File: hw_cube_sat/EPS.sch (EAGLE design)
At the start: 0 parts

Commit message: added sections for eps sch
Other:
- note added: "3V REFERENCE"
- note added: "3V3 REGULATOR"
- note added: "BATTERY + BATTERY CHARGER"
- note added: "HIGH-LEVEL ARCHITECTURE"
- note added: "POWER MANAGEMENT MICROCONTROLLER"
- note added: "SOLAR ARRAY + MPPT"
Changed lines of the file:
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@@
 <setting verticaltext="up"/>
 </settings>
-<grid distance="0.1" unitdist="inch" unit="inch" style="lines" multiple="1" display="no" altdistance="0.01" altunitdist="inch" altunit="inch"/>
+<grid distance="0.1" unitdist="inch" unit="inch" style="lines" multiple="1" display="yes" altdistance="0.01" altunitdist="inch" altunit="inch"/>
 <layers>
 <layer number="1" name="Top" color="4" fill="1" visible="no" active="no"/>
@@
 <parts>
 <part name="FRAME1" library="frames" library_urn="urn:adsk.eagle:library:229" deviceset="A3L-LOC" device=""/>
+<part name="FRAME2" library="frames" library_urn="urn:adsk.eagle:library:229" deviceset="A3L-LOC" device=""/>
+<part name="FRAME3" library="frames" library_urn="urn:adsk.eagle:library:229" deviceset="A3L-LOC" device=""/>
 </parts>
 <sheets>
 <sheet>
 <plain>
+<text x="7.62" y="248.92" size="2.54" layer="94">HIGH-LEVEL ARCHITECTURE</text>
+</plain>
+<instances>
+<instance part="FRAME2" gate="G$1" x="0" y="0" smashed="yes">
+<attribute name="DRAWING_NAME" x="344.17" y="15.24" size="2.54" layer="94"/>
+<attribute name="LAST_DATE_TIME" x="344.17" y="10.16" size="2.286" layer="94"/>
+<attribute name="SHEET" x="357.505" y="5.08" size="2.54" layer="94"/>
+</instance>
+</instances>
+<busses>
+</busses>
+<nets>
+</nets>
+</sheet>
+<sheet>
+<plain>
+<wire x1="241.3" y1="139.7" x2="241.3" y2="254" width="0.1524" layer="94"/>
+<text x="10.16" y="248.92" size="2.54" layer="94">SOLAR ARRAY + MPPT</text>
+<wire x1="241.3" y1="139.7" x2="381" y2="139.7" width="0.1524" layer="94"/>
+<text x="246.38" y="248.92" size="2.54" layer="94">BATTERY + BATTERY CHARGER</text>
+<wire x1="241.3" y1="139.7" x2="241.3" y2="5.08" width="0.1524" layer="94"/>
+<text x="246.38" y="129.54" size="2.54" layer="94">3V3 REGULATOR</text>
+<text x="246.38" y="78.74" size="2.54" layer="94">3V REFERENCE</text>
 </plain>
 <instances>
@@
 <attribute name="DRAWING_NAME" x="344.17" y="15.24" size="2.54" layer="94"/>
 <attribute name="LAST_DATE_TIME" x="344.17" y="10.16" size="2.286" layer="94"/>
+<attribute name="SHEET" x="357.505" y="5.08" size="2.54" layer="94"/>
+</instance>
+</instances>
+<busses>
+</busses>
+<nets>
+</nets>
+</sheet>
+<sheet>
+<plain>
+<text x="12.7" y="246.38" size="2.54" layer="94">POWER MANAGEMENT MICROCONTROLLER</text>
+</plain>
+<instances>
+<instance part="FRAME3" gate="G$1" x="0" y="0" smashed="yes">
+<attribute name="DRAWING_NAME" x="344.17" y="15.24" size="2.54" layer="94"/>
+<attribute name="LAST_DATE_TIME" x="344.17" y="10.16" size="2.286" layer="94"/>

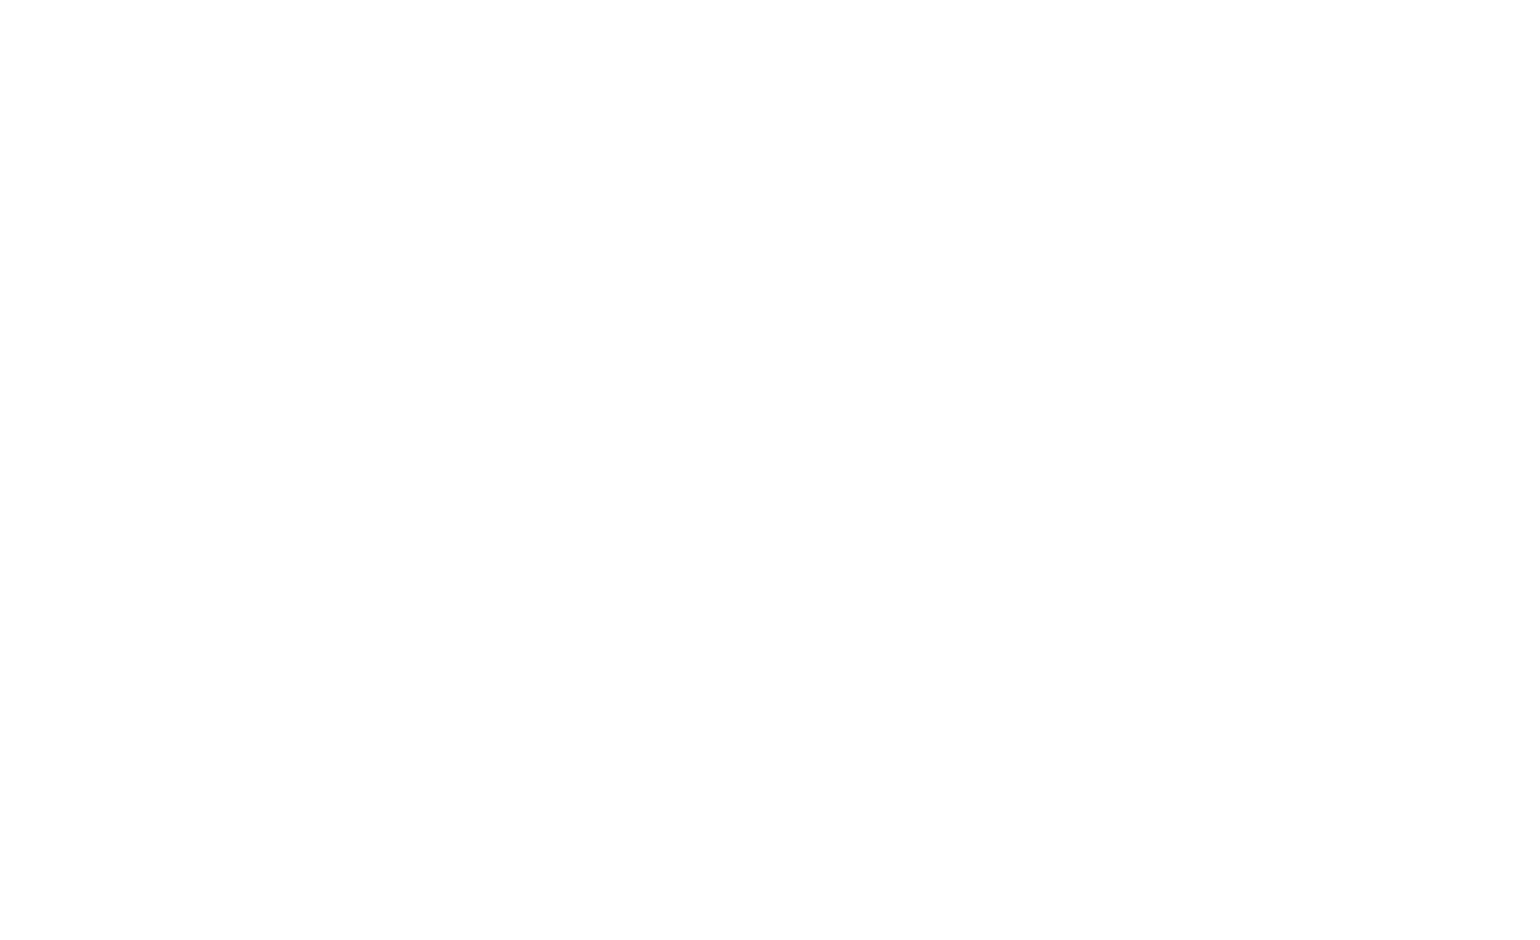
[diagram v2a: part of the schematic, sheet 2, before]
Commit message: Added LT3652 to schematic
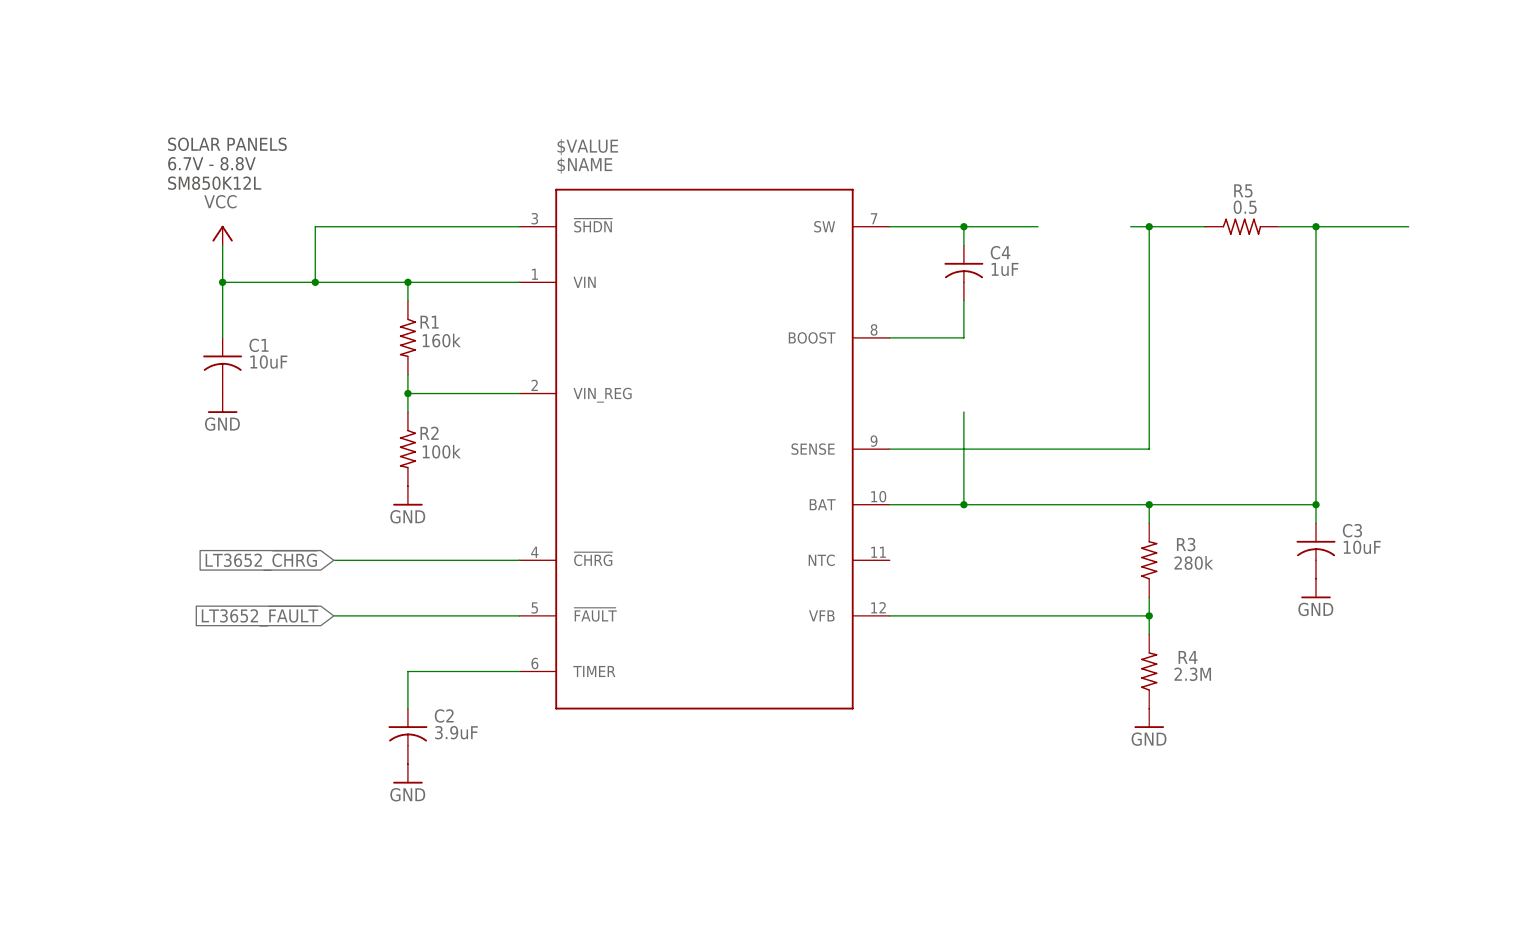
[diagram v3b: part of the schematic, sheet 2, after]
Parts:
- added C1, C3: 10uF, rcl:C-USC0603
- added C2: 3.9uF, rcl:C-USC0603
- added C4: 1uF, rcl:C-USC0603
- added R1: 160k, rcl:R-US_R0603
- added R2: 100k, rcl:R-US_R0603
- added R3: 280k, rcl:R-US_R0603
- added R4: 2.3M, rcl:R-US_R0603
- added R5: 0.5, rcl:R-US_R0603
- added U$1: LT3652, cube-sat:LT3652
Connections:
- new net GND: C1.2, C2.2, C3.2, R2.2, R4.1
- new net LT3652_!CHRG: U$1.!CHRG
- new net LT3652_!FAULT: U$1.!FAULT
- new net N$1: R1.2, R2.1, U$1.VIN_REG
- new net N$2: R3.1, R4.2, U$1.VFB
- new net N$3: C2.1, U$1.TIMER
- new net N$4: C3.1, R3.2, R5.2, U$1.BAT
- new net N$5: R5.1, U$1.SENSE
- new net N$6: C4.2, U$1.BOOST
- new net N$7: C4.1, U$1.SW
- new net VCC: C1.1, R1.1, U$1.!SHDN, U$1.VIN
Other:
- note added: "SOLAR PANELS 6.7V - 8.8V SM850K12L"

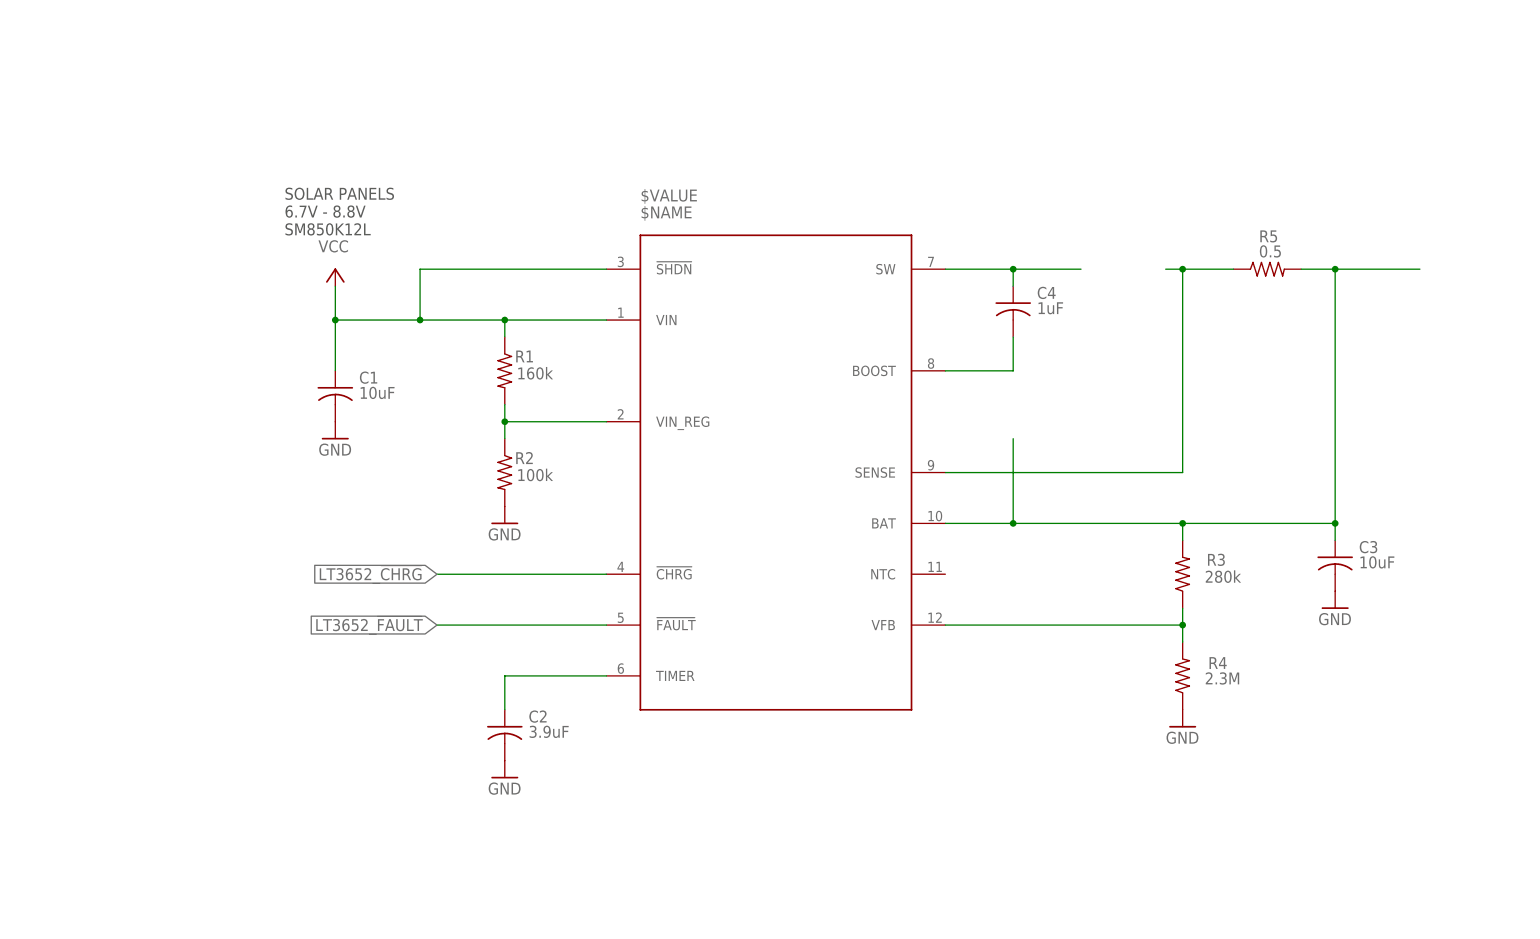
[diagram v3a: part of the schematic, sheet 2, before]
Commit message: Finished LT3652
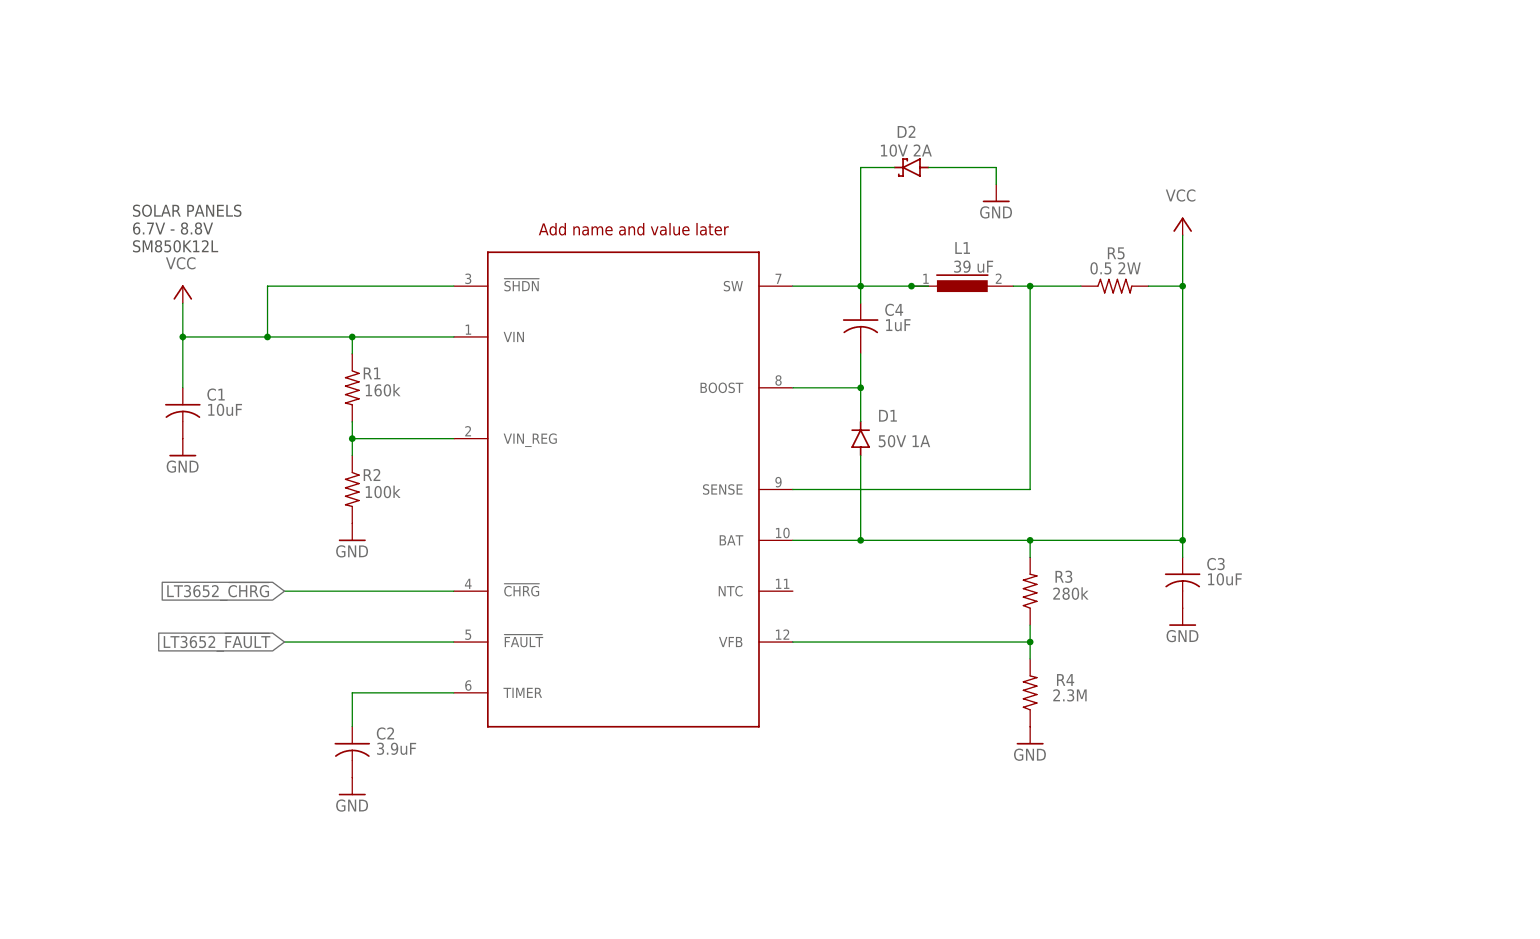
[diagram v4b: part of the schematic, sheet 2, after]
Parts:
- added D1: 50V 1A, diode:GF1
- added D2: 10V 2A, diode:BAT60J
- added L1: 39 uF, inductors:B82132
- R5: value 0.5 -> 0.5 2W; device rcl:R-US_R0603 -> rcl:R-US_R2512W
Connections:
- removed net N$4: C3.1, R3.2, R5.2, U$1.BAT
- net GND: now also D2.A
- net N$5: now also L1.2
- net N$6: now also D1.C
- net N$7: now also D2.C, L1.1
- net VCC: now also C3.1, D1.A, R3.2, R5.2, U$1.BAT
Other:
- note added: "Add name and value later"
- moved on the sheet: C1, C2, C3, C4, R1, R2, R3, R4, R5
